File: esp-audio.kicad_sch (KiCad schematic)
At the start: 75 parts, among them J1 PJ-342B, J2 HR911105A, J3 USB_C_Receptacle_USB2.0, J4 Conn_01x03_Socket, J5 Conn_01x12_Pin, SW1 SW_Push, SW2 SW_Push, U1 W5500, U10 MT2492, U2 ESP32-S3-WROOM-1U-N8R8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

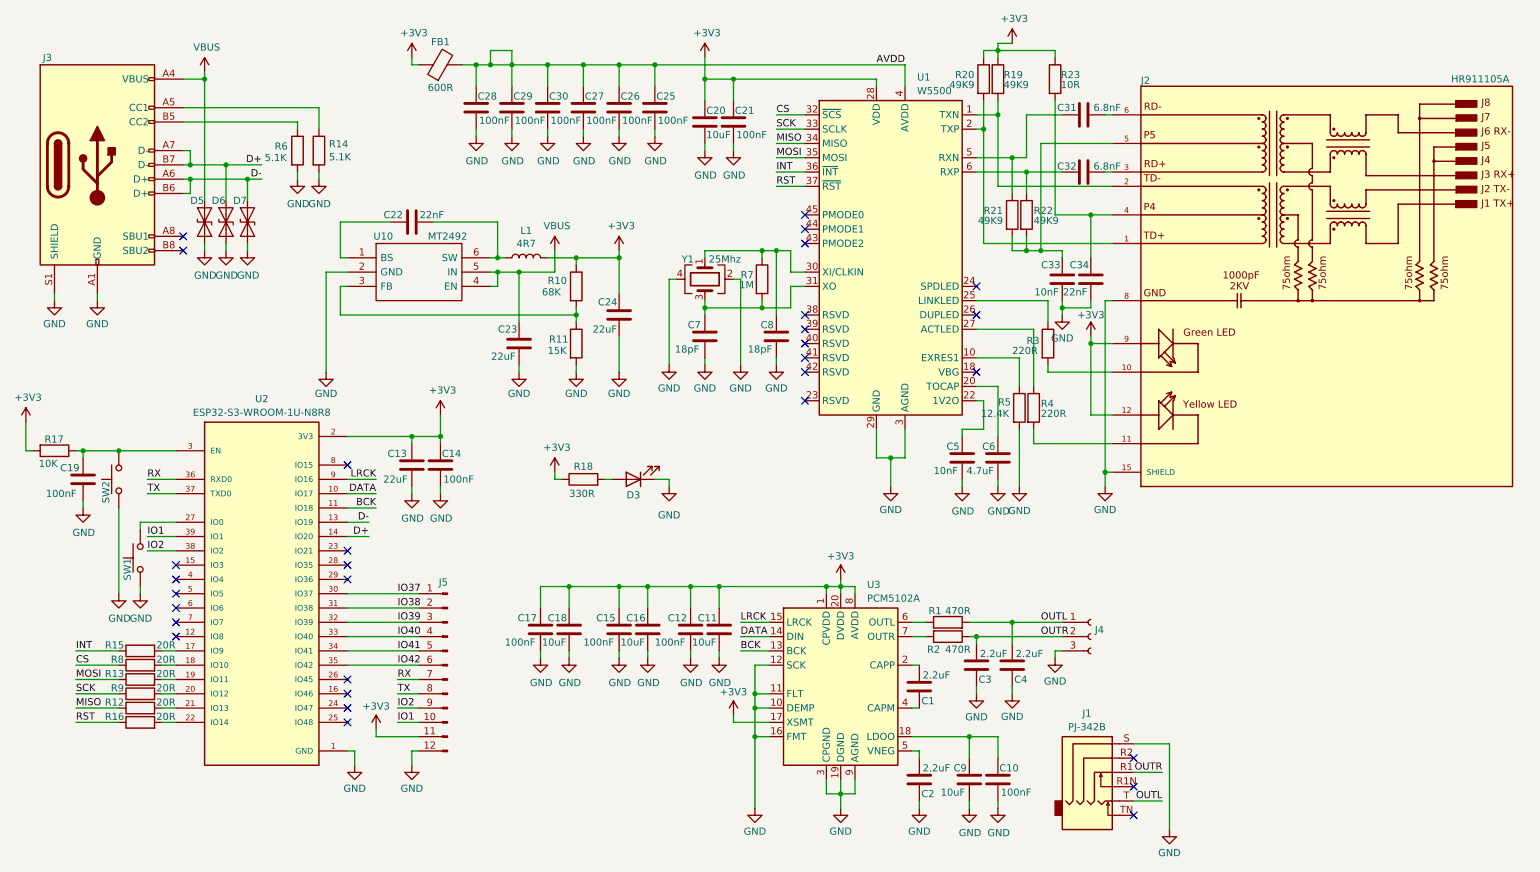
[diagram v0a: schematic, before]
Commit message: fix USB D+/D-, caps, add power pins
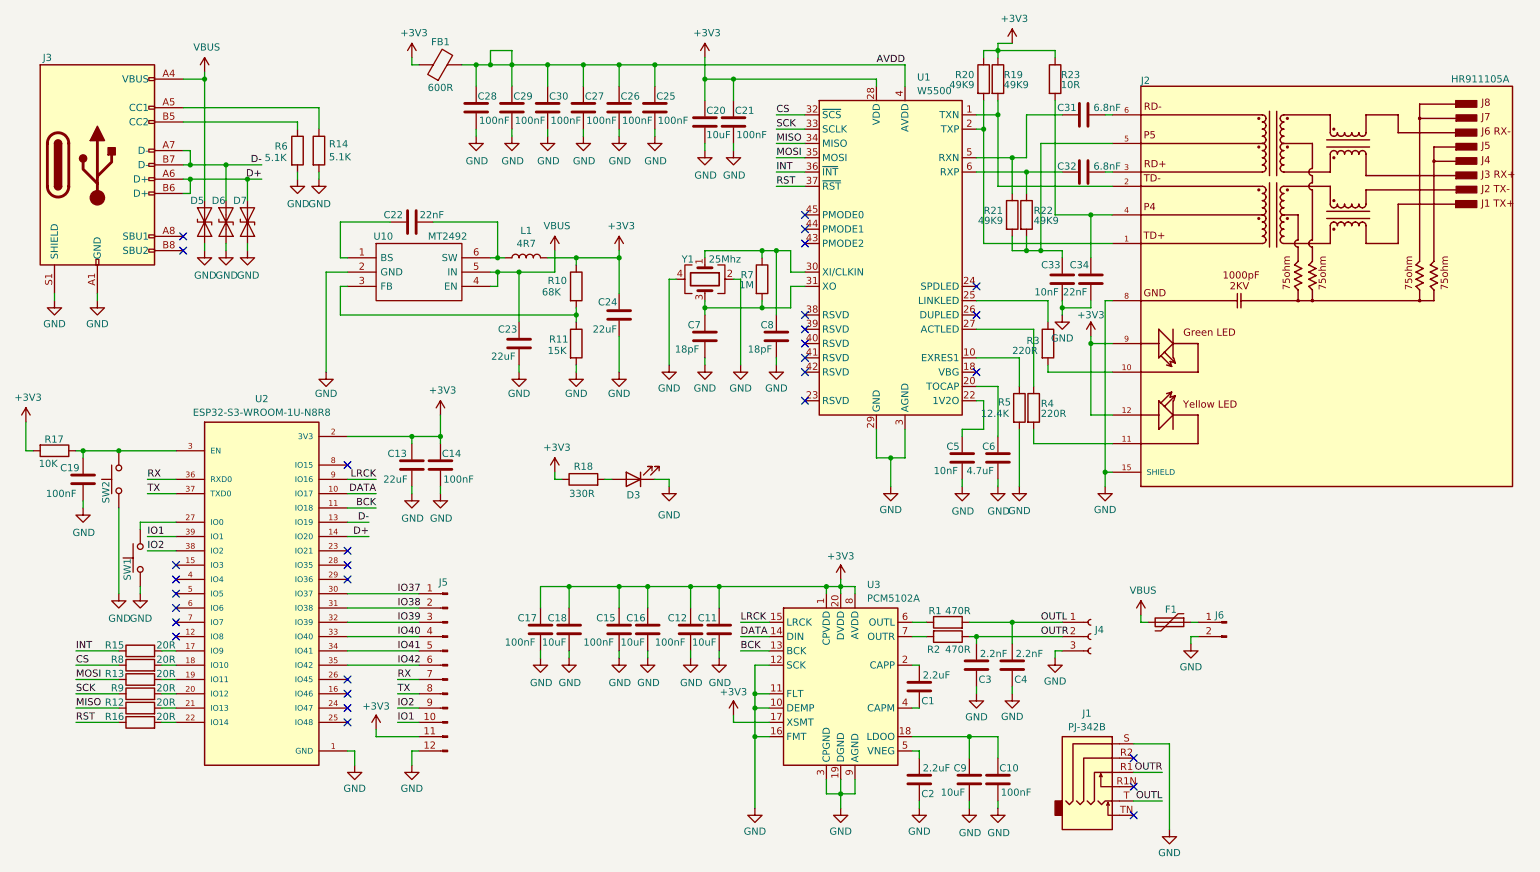
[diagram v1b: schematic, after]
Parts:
- added F1: 3A 12V, Fuse:Fuse_1206_3216Metric, symbol Device:Polyfuse
- added J6: Conn_01x02_Pin, Connector_PinHeader_2.54mm:PinHeader_1x02_P2.54mm_Vertical, symbol Connector:Conn_01x02_Pin
- C3, C4: value 2.2uF -> 2.2nF; LCSC C23630 -> C1604
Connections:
- net D+: now also D7.1 (A1), J3.A6 (D+), J3.B6 (D+); no longer D6.1 (A1), J3.A7 (D-), J3.B7 (D-)
- net D-: now also D6.1 (A1), J3.A7 (D-), J3.B7 (D-); no longer D7.1 (A1), J3.A6 (D+), J3.B6 (D+)
- net GND: now also J6.2 (Pin_2)
- net VBUS: now also F1.2
- new net: F1.1, J6.1 (Pin_1)

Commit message: fixed save
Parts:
- added J7: Conn_01x02_Pin, Connector_PinHeader_2.54mm:PinHeader_1x02_P2.54mm_Vertical, symbol Connector:Conn_01x02_Pin
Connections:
- net OUTL: now also J7.2 (Pin_2)
- net OUTR: now also J7.1 (Pin_1)
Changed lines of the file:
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@@
 	)
 	(junction
+		(at 214.63 147.32)
+		(diameter 0)
+		(color 0 0 0 0)
+	)
+	(junction
 		(at 160.02 114.3)
 		(diameter 0)
@@
 	)
 	(junction
+		(at 214.63 152.4)
+		(diameter 0)
+		(color 0 0 0 0)
+	)
+	(junction
 		(at 160.02 151.13)
 		(diameter 0)
@@
 	(wire
 		(pts
+			(xy 212.09 147.32) (xy 214.63 147.32)
+		)
+		(stroke
+			(width 0)
+			(type default)
+		)
+	)
+	(wire
+		(pts
 			(xy 39.37 133.35) (xy 41.91 133.35)
 		)
@@
 	(wire
 		(pts
+			(xy 214.63 152.4) (xy 227.33 152.4)
+		)
+		(stroke
+			(width 0)
+			(type default)
+		)
+	)
+	(wire
+		(pts
 			(xy 184.15 68.58) (xy 194.31 68.58)
 		)
@@
 	(wire
 		(pts
-			(xy 212.09 147.32) (xy 217.17 147.32)
-		)
-		(stroke
-			(width 0)
-			(type default)
-		)
-	)
-	(wire
-		(pts
 			(xy 127 34.29) (xy 127 33.02)
 		)
@@
 	(wire
 		(pts
-			(xy 218.44 142.24) (xy 218.44 157.48)
+			(xy 157.48 115.57) (xy 157.48 114.3)
 		)
 		(stroke
@@
 	(wire
 		(pts
-			(xy 157.48 115.57) (xy 157.48 114.3)
+			(xy 187.96 153.67) (xy 187.96 152.4)
 		)
 		(stroke
@@
 	(wire
 		(pts
-			(xy 187.96 153.67) (xy 187.96 152.4)
+			(xy 72.39 115.57) (xy 85.09 115.57)
 		)
 		(stroke
@@
 	(wire
 		(pts
-			(xy 72.39 115.57) (xy 85.09 115.57)
+			(xy 187.96 30.48) (xy 187.96 43.18)
 		)
 		(stroke
@@
 	(wire
 		(pts
-			(xy 187.96 30.48) (xy 187.96 43.18)
+			(xy 106.68 114.3) (xy 106.68 118.11)
 		)
 		(stroke
@@
 	(wire
 		(pts
-			(xy 106.68 114.3) (xy 106.68 118.11)
+			(xy 214.63 149.86) (xy 214.63 152.4)
 		)
 		(stroke
@@
 	(wire
 		(pts
-			(xy 212.09 152.4) (xy 217.17 152.4)
-		)
-		(stroke
-			(width 0)
-			(type default)
-		)
-	)
-	(wire
-		(pts
 			(xy 77.47 97.79) (xy 72.39 97.79)
 		)
@@
 	(wire
 		(pts
+			(xy 214.63 152.4) (xy 212.09 152.4)
+		)
+		(stroke
+			(width 0)
+			(type default)
+		)
+	)
+	(wire
+		(pts
 			(xy 44.45 44.45) (xy 44.45 41.91)
 		)
@@
 	(wire
 		(pts
+			(xy 228.6 142.24) (xy 228.6 157.48)
+		)
+		(stroke
+			(width 0)
+			(type default)
+		)
+	)
+	(wire
+		(pts
 			(xy 140.97 36.83) (xy 140.97 35.56)
 		)
@@
 	(wire
 		(pts
-			(xy 212.09 142.24) (xy 218.44 142.24)
+			(xy 212.09 142.24) (xy 228.6 142.24)
 		)
 		(stroke
@@
 	(wire
 		(pts
+			(xy 214.63 147.32) (xy 227.33 147.32)
+		)
+		(stroke
+			(width 0)
+			(type default)
+		)
+	)
+	(wire
+		(pts
 			(xy 81.28 138.43) (xy 85.09 138.43)
 		)
@@
 	)
 	(label "OUTR"
-		(at 217.17 147.32 180)
+		(at 227.33 147.32 180)
 		(effects
 			(font
@@
 	)
 	(label "OUTL"
-		(at 217.17 152.4 180)
+		(at 227.33 152.4 180)
 		(effects
 			(font
@@
 	(symbol
 		(lib_id "power:GND")
-		(at 218.44 157.48 0)
+		(at 228.6 157.48 0)
 		(unit 1)
 		(body_style 1)
@@
 		(fields_autoplaced yes)
 		(property "Reference" "#PWR08"
-			(at 218.44 163.83 0)
+			(at 228.6 163.83 0)
 			(hide yes)
 			(show_name no)
@@
 		)
 		(property "Value" "GND"
-			(at 218.44 161.6131 0)
+			(at 228.6 161.6131 0)
 			(show_name no)
 			(do_not_autoplace no)
@@
 		)
 		(property "Footprint" ""
-			(at 218.44 157.48 0)
+			(at 228.6 157.48 0)
 			(hide yes)
 			(show_name no)
@@
 		)
 		(property "Datasheet" ""
-			(at 218.44 157.48 0)
+			(at 228.6 157.48 0)
 			(hide yes)
 			(show_name no)
@@
 		)
 		(property "Description" "Power symbol creates a global label with name \"GND\" , ground"
-			(at 218.44 157.48 0)
+			(at 228.6 157.48 0)
 			(hide yes)
 			(show_name no)
@@
 					(unit 1)
 				)
+			)
+		)
+	)
+	(symbol
+		(lib_id "Connector:Conn_01x02_Pin")
+		(at 219.71 147.32 0)
+		(mirror y)
+		(unit 1)
+		(body_style 1)
+		(exclude_from_sim no)
+		(in_bom no)
+		(on_board yes)
+		(in_pos_files yes)
+		(dnp no)
+		(property "Reference" "J7"
+			(at 218.44 146.05 0)
+			(show_name no)
+			(do_not_autoplace no)
+			(effects
+				(font
+					(size 1.27 1.27)
+				)
+			)
+		)
+		(property "Value" "Conn_01x02_Pin"
+			(at 219.075 144.78 0)
+			(hide yes)
+			(show_name no)
+			(do_not_autoplace no)
+			(effects
+				(font
+					(size 1.27 1.27)
+				)
+			)
+		)
+		(property "Footprint" "Connector_PinHeader_2.54mm:PinHeader_1x02_P2.54mm_Vertical"
+			(at 219.71 147.32 0)
+			(hide yes)
+			(show_name no)
+			(do_not_autoplace no)
+			(effects
+				(font
+					(size 1.27 1.27)
+				)
+			)
+		)
+		(property "Datasheet" ""
+			(at 219.71 147.32 0)
+			(hide yes)
+			(show_name no)
+			(do_not_autoplace no)
+			(effects
+				(font
+					(size 1.27 1.27)
+				)
+			)
+		)
+		(property "Description" "Generic connector, single row, 01x02, script generated"
+			(at 219.71 147.32 0)
+			(hide yes)
+			(show_name no)
+			(do_not_autoplace no)
+			(effects
+				(font
+					(size 1.27 1.27)
+				)
+			)
+		)
+		(pin "1"
+		)
+		(pin "2"
+		)
+		(instances
+			(project "esp-audio"
+				(path "/9de7b2ec-eebd-4141-baff-56ff3aceffa9"
+					(reference "J7")
+					(unit 1)
+				)
